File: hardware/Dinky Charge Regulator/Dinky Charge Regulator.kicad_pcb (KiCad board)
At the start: 2 copper layers, 69 x 36 mm, 12 parts, among them Q101 2SC5354

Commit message: addedldvnldt
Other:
- board text added: "BJT voltage regulator, (120, 700)V in ~120V out"

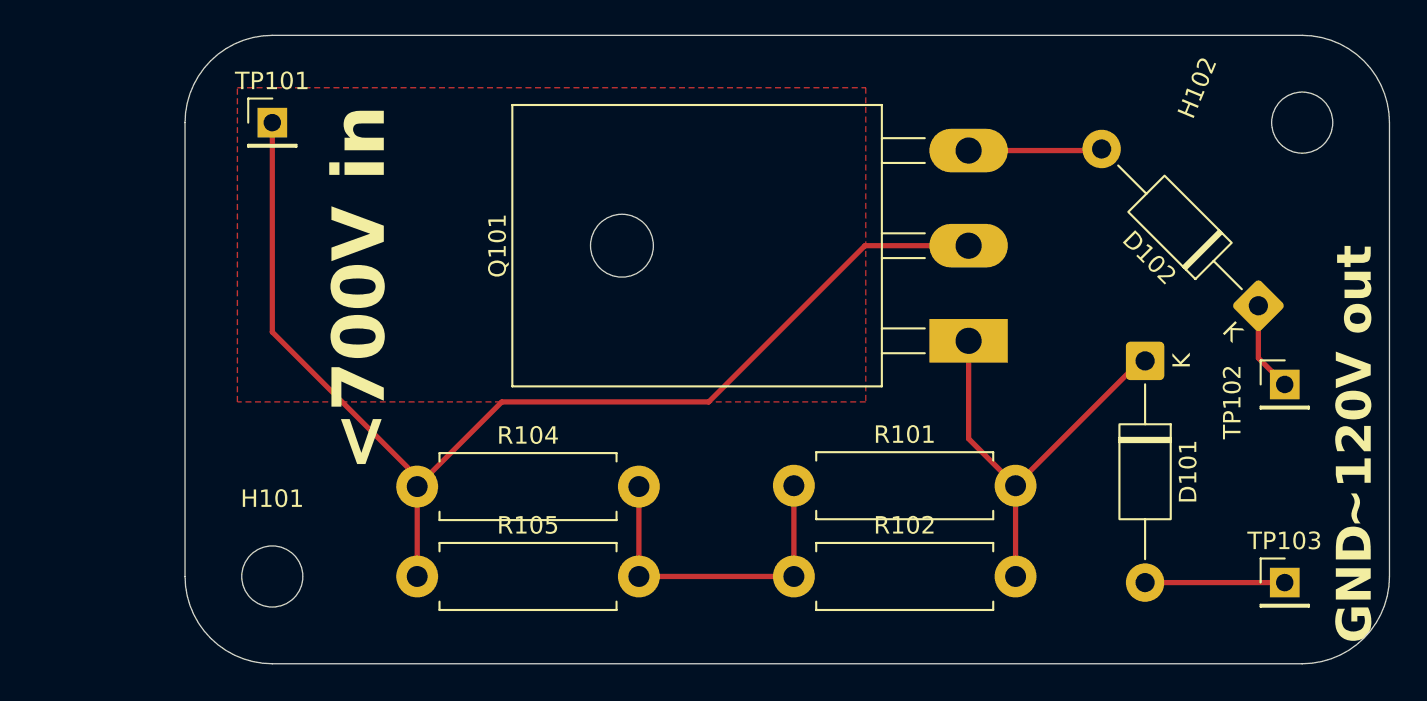
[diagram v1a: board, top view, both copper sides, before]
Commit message: dinkified charger
even dinkier than before. (with extra warning stickers)
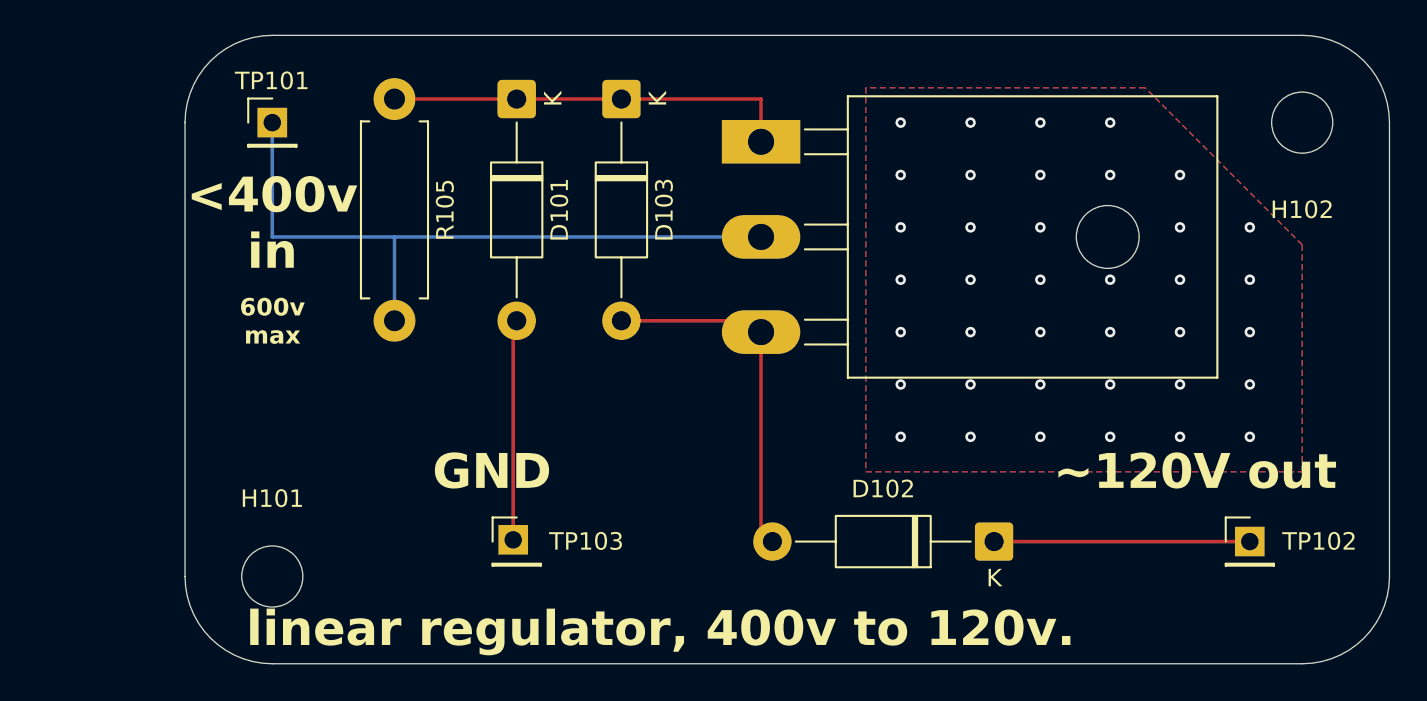
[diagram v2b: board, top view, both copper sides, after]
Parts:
- removed R101, R102, R104: 20k, Resistor_THT:R_Axial_DIN0411_L9.9mm_D3.6mm_P12.70mm_Horizontal
- added D103: 15, Diode_THT:D_DO-41_SOD81_P12.70mm_Horizontal, F.Cu at (161.0, 92.7)
- Q101: value 2SC5354 -> Q_NMOS
- R105: value 20k -> 680k
- moved TP103 44.1 mm to (155.0, 118.0)
- moved D101 39.0 mm to (155.0, 92.7)
- moved R105 27.4 mm to (148.0, 92.7), turned to -90 degrees
- moved D102 20.3 mm to (182.3, 118.0), turned to 180 degrees
- moved Q101 16.5 mm to (169.0, 95.1), turned to -90 degrees
- moved TP102 9.22 mm to (197.0, 118.0)
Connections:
- R105 pad 1: VBUS -> Net-(D101-K)
- R105 pad 2: Net-(R101-Pad1) -> VBUS
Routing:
- net VBUS: track 66.7 -> 39.4 mm
- net Net-(R101-Pad1): track 19.2 -> 0.00 mm
- net Net-(D102-A): track 7.66 -> 21.5 mm
- net +BATT: track 5.14 -> 14.7 mm
- net GND: track 7.00 -> 12.6 mm
- net Net-(D101-K): track 25.0 -> 23.5 mm, vias 0 -> 38
- added copper zone on B.Cu, net Net-(D101-K)
- added copper zone on F.Cu, net Net-(D101-K)
- removed copper zone on F.Cu, net (none)
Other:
- board text added: "600v max"
- board text added: "<400v in"
- board text added: "linear regulator, 400v to 120v."
- board text added: "monitor for overheating"
- board text removed: "<700V in"
- board text removed: "BJT voltage regulator, (120, 700)V in ~120V out"
